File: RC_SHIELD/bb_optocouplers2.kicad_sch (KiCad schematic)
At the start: 20 parts, among them J1 Conn_01x04, U1 SFH6345, U2 SFH6345

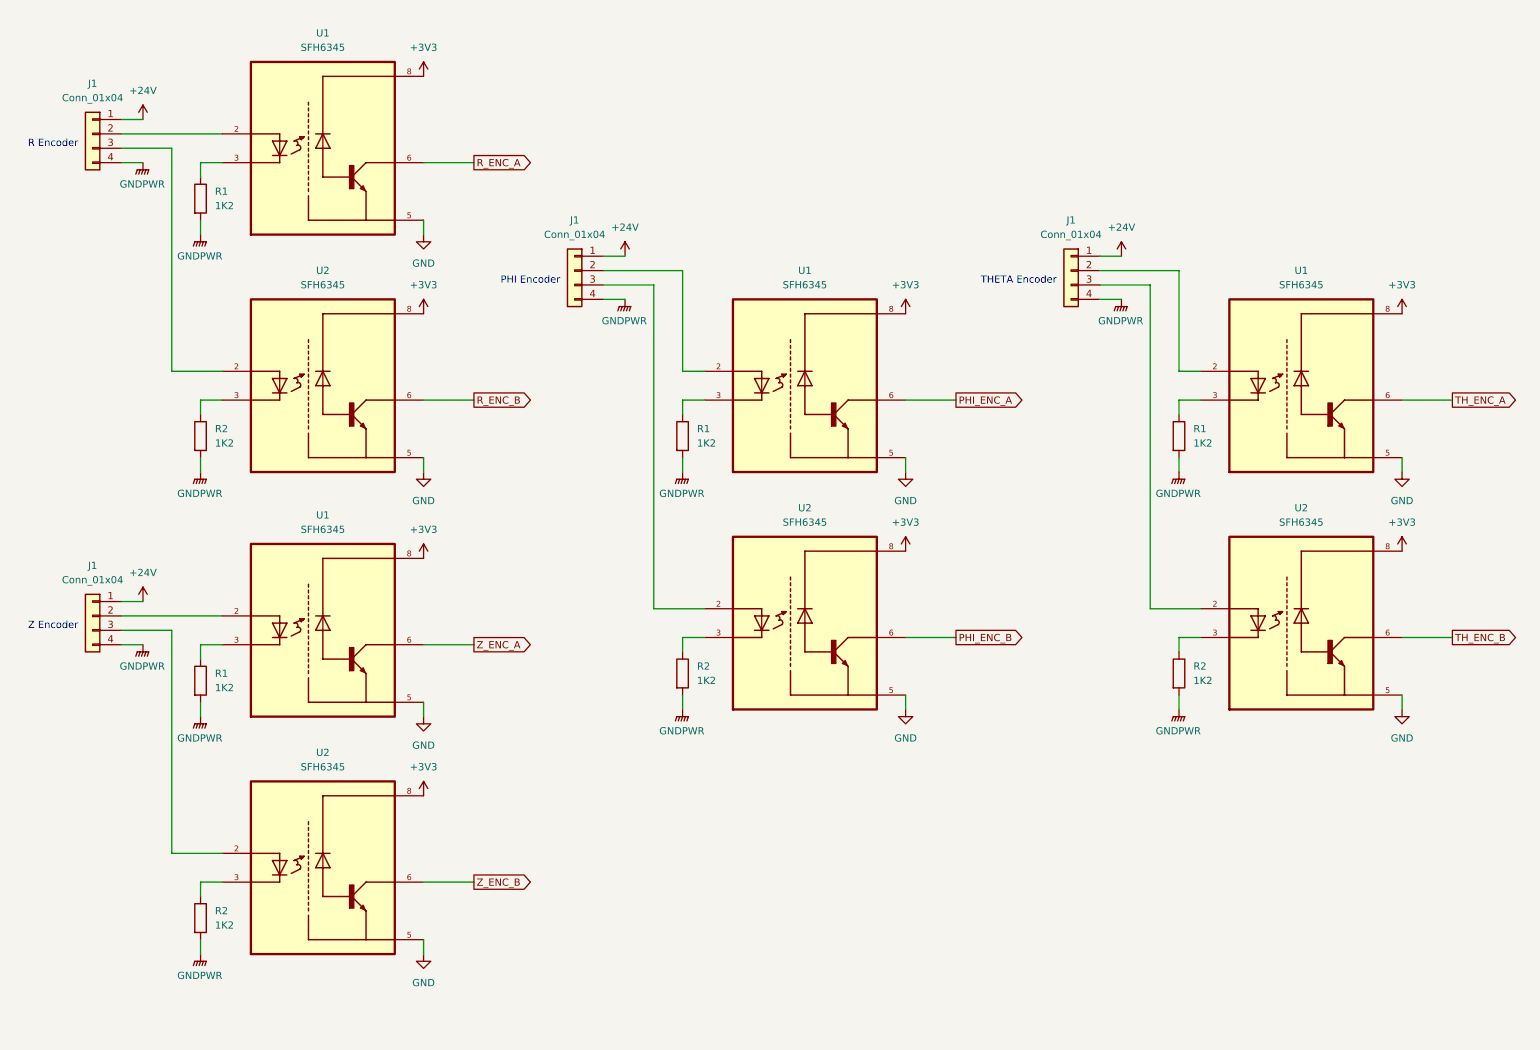
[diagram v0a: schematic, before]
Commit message: added secondary MCU to schematic and made it more consistent
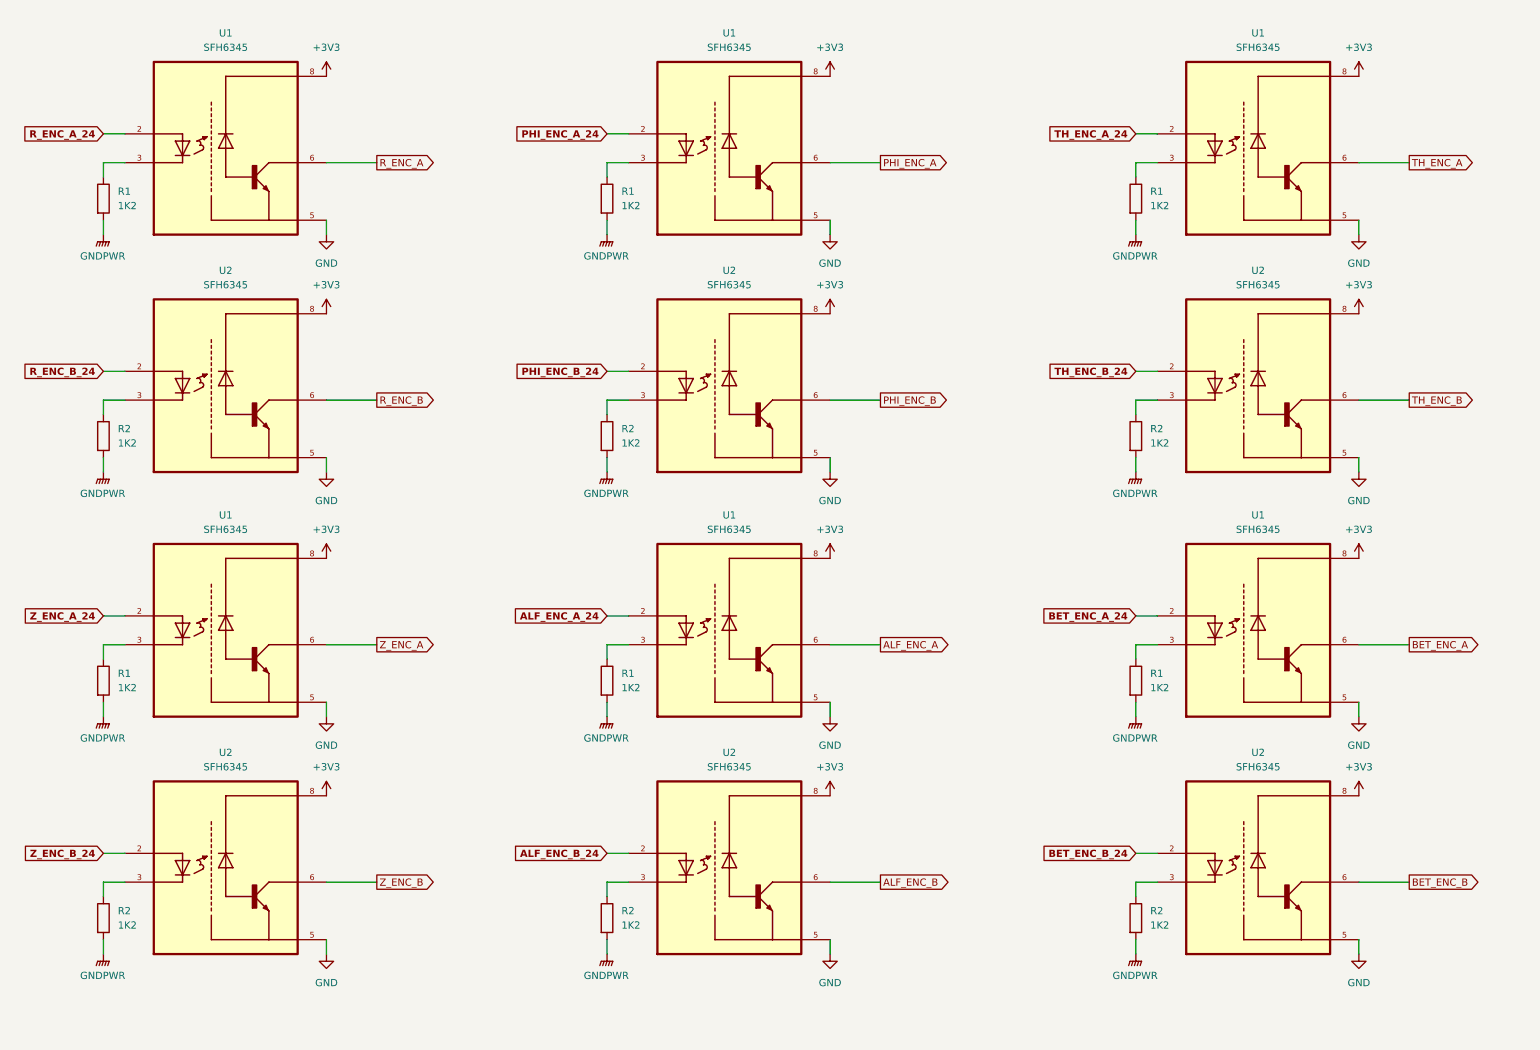
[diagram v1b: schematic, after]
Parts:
- removed J1 (x4): Conn_01x04, Connector_RJ:RJ9_Evercom_5301-440xxx_Horizontal, symbol Connector_Generic:Conn_01x04
- added R1 (x2), R2 (x2): 1K2, symbol Device:R
- added U1 (x2), U2 (x2): SFH6345, SFH6345:DIP762W50P254L977H451Q8, symbol SFH6345:SFH6345
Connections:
- net +3V3: now also U1.8, U1.8, U2.8, U2.8
- net GND: now also U1.5, U1.5, U2.5, U2.5
- net GNDPWR: now also R1.2, R1.2, R2.2, R2.2
- net PHI_ENC_B_24: now reaches U2.2
- net PHI_ENC_A_24: now reaches U1.2
- net TH_ENC_A_24: now reaches U1.2
- net Z_ENC_A_24: now reaches U1.2
- net R_ENC_A_24: now reaches U1.2
- net R_ENC_B_24: now reaches U2.2
- net Z_ENC_B_24: now reaches U2.2
- net TH_ENC_B_24: now reaches U2.2
- new net: R1.1, U1.3 (x2)
- new net: R2.1, U2.3 (x2)
- new net ALF_ENC_A: U1.6
- new net ALF_ENC_A_24: U1.2
- new net ALF_ENC_B: U2.6
- new net ALF_ENC_B_24: U2.2
- new net BET_ENC_A: U1.6
- new net BET_ENC_A_24: U1.2
- new net BET_ENC_B: U2.6
- new net BET_ENC_B_24: U2.2
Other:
- note removed: "PHI Encoder"
- note removed: "R Encoder"
- note removed: "THETA Encoder"
- note removed: "Z Encoder"
- company: (none) -> LEGO Kör (legokor.hu)
- title: ENCODERS -> Karcsi (INDACT Robot Arm) - Encoder optocouplers
- moved on the sheet: R1, R2, U1, U2

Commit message: footprints assigned
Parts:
- R1, R2: footprint (none) -> Resistor_SMD:R_0805_2012Metric_Pad1.20x1.40mm_HandSolder
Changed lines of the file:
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@@
       (effects (font (size 1.27 1.27)) (justify left))
     )
-    (property "Footprint" "" (at 209.042 45.72 90)
+    (property "Footprint" "Resistor_SMD:R_0805_2012Metric_Pad1.20x1.40mm_HandSolder" (at 209.042 45.72 90)
       (effects (font (size 1.27 1.27)) hide)
     )
@@
       (effects (font (size 1.27 1.27)) (justify left))
     )
-    (property "Footprint" "" (at 26.797 87.63 90)
+    (property "Footprint" "Resistor_SMD:R_0805_2012Metric_Pad1.20x1.40mm_HandSolder" (at 26.797 87.63 90)
       (effects (font (size 1.27 1.27)) hide)
     )
@@
       (effects (font (size 1.27 1.27)) (justify left))
     )
-    (property "Footprint" "" (at 115.697 87.63 90)
+    (property "Footprint" "Resistor_SMD:R_0805_2012Metric_Pad1.20x1.40mm_HandSolder" (at 115.697 87.63 90)
       (effects (font (size 1.27 1.27)) hide)
     )
@@
       (effects (font (size 1.27 1.27)) (justify left))
     )
-    (property "Footprint" "" (at 209.042 87.63 90)
+    (property "Footprint" "Resistor_SMD:R_0805_2012Metric_Pad1.20x1.40mm_HandSolder" (at 209.042 87.63 90)
       (effects (font (size 1.27 1.27)) hide)
     )
@@
       (effects (font (size 1.27 1.27)) (justify left))
     )
-    (property "Footprint" "" (at 209.042 172.72 90)
+    (property "Footprint" "Resistor_SMD:R_0805_2012Metric_Pad1.20x1.40mm_HandSolder" (at 209.042 172.72 90)
       (effects (font (size 1.27 1.27)) hide)
     )
@@
       (effects (font (size 1.27 1.27)) (justify left))
     )
-    (property "Footprint" "" (at 209.042 130.81 90)
+    (property "Footprint" "Resistor_SMD:R_0805_2012Metric_Pad1.20x1.40mm_HandSolder" (at 209.042 130.81 90)
       (effects (font (size 1.27 1.27)) hide)
     )
@@
       (effects (font (size 1.27 1.27)) (justify left))
     )
-    (property "Footprint" "" (at 115.697 45.72 90)
+    (property "Footprint" "Resistor_SMD:R_0805_2012Metric_Pad1.20x1.40mm_HandSolder" (at 115.697 45.72 90)
       (effects (font (size 1.27 1.27)) hide)
     )
@@
       (effects (font (size 1.27 1.27)) (justify left))
     )
-    (property "Footprint" "" (at 26.797 45.72 90)
+    (property "Footprint" "Resistor_SMD:R_0805_2012Metric_Pad1.20x1.40mm_HandSolder" (at 26.797 45.72 90)
       (effects (font (size 1.27 1.27)) hide)
     )
@@
       (effects (font (size 1.27 1.27)) (justify left))
     )
-    (property "Footprint" "" (at 115.697 172.72 90)
+    (property "Footprint" "Resistor_SMD:R_0805_2012Metric_Pad1.20x1.40mm_HandSolder" (at 115.697 172.72 90)
       (effects (font (size 1.27 1.27)) hide)
     )
@@
       (effects (font (size 1.27 1.27)) (justify left))
     )
-    (property "Footprint" "" (at 115.697 130.81 90)
+    (property "Footprint" "Resistor_SMD:R_0805_2012Metric_Pad1.20x1.40mm_HandSolder" (at 115.697 130.81 90)
       (effects (font (size 1.27 1.27)) hide)
     )
@@
       (effects (font (size 1.27 1.27)) (justify left))
     )
-    (property "Footprint" "" (at 26.797 172.72 90)
+    (property "Footprint" "Resistor_SMD:R_0805_2012Metric_Pad1.20x1.40mm_HandSolder" (at 26.797 172.72 90)
       (effects (font (size 1.27 1.27)) hide)
     )
@@
       (effects (font (size 1.27 1.27)) (justify left))
     )
-    (property "Footprint" "" (at 26.797 130.81 90)
-      (effects (font (size 1.27 1.27)) hide)
-    )
+    (property "Footprint" "Resistor_SMD:R_0805_2012Metric_Pad1.20x1.40mm_HandSolder" (at 26.797 130.81 90)
+      (effects (font (size 1.27 1.27)) hide)
+    )

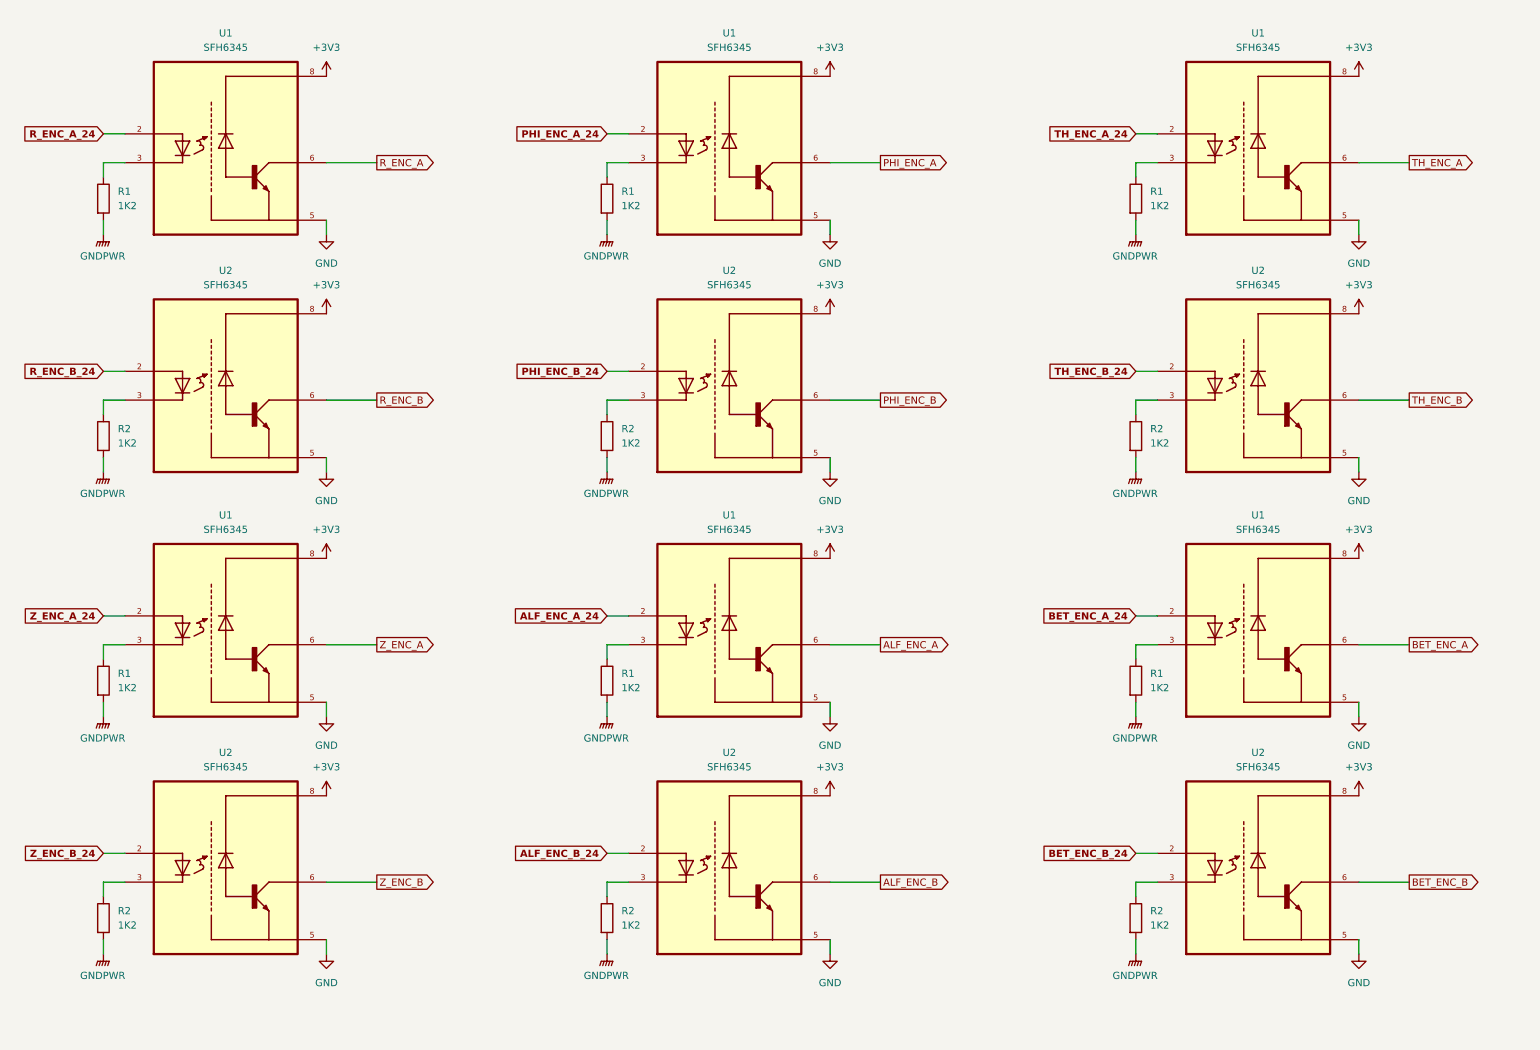
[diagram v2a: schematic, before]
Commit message: Fixed typos and names in schematic, changed optocoupler resistors; added .gitgnore file
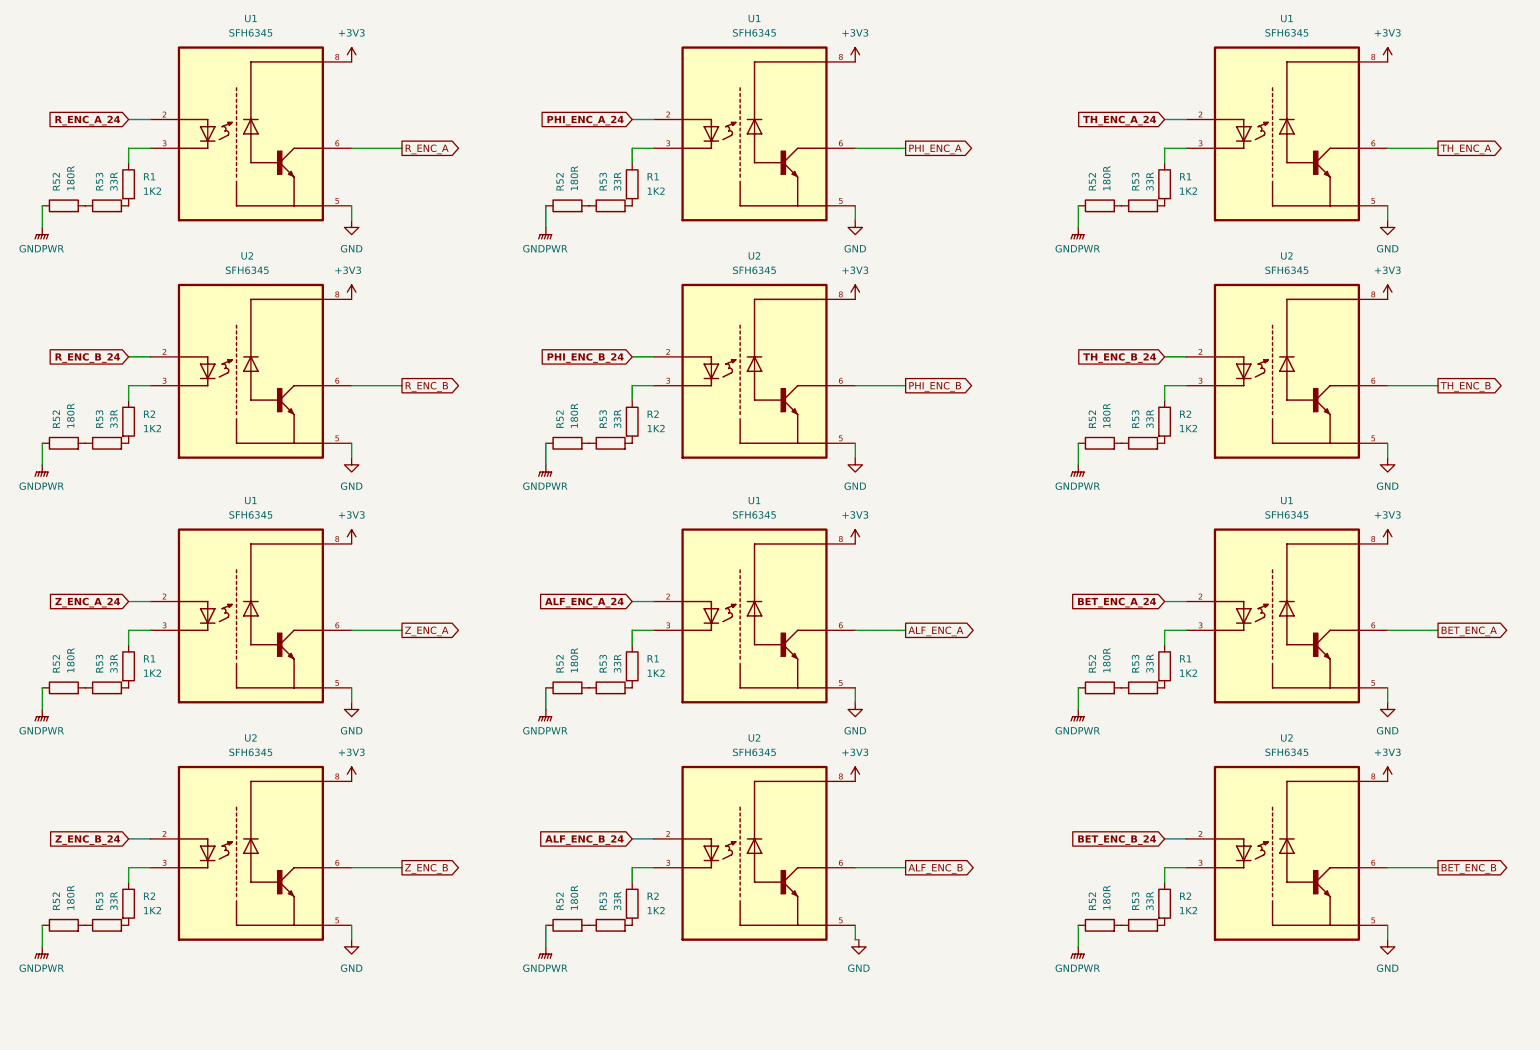
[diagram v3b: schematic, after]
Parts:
- added R52 (x12): 180R, Resistor_SMD:R_0805_2012Metric_Pad1.20x1.40mm_HandSolder, symbol Device:R
- added R53 (x12): 33R, Resistor_SMD:R_0805_2012Metric_Pad1.20x1.40mm_HandSolder, symbol Device:R
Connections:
- net GNDPWR: now also R52.1, R52.1, R52.1, R52.1, R52.1, R52.1, R52.1, R52.1, R52.1, R52.1, R52.1, R52.1; no longer R1.2, R1.2, R1.2, R1.2, R1.2, R1.2, R2.2, R2.2, R2.2, R2.2, R2.2, R2.2
- new net: R52.2, R53.1 (x12)
- new net: R2.2, R53.2 (x6)
- new net: R1.2, R53.2 (x6)
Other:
- moved on the sheet: R1, R2, U1, U2
